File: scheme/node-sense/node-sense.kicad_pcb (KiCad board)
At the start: 2 copper layers, 33.5 x 33 mm, 20 parts, among them P1 Power, P10 CN, P11 CN, P12 CN, P13 CN, P2 CN, P3 CN, P4 CN, P6 CN, P8 CN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

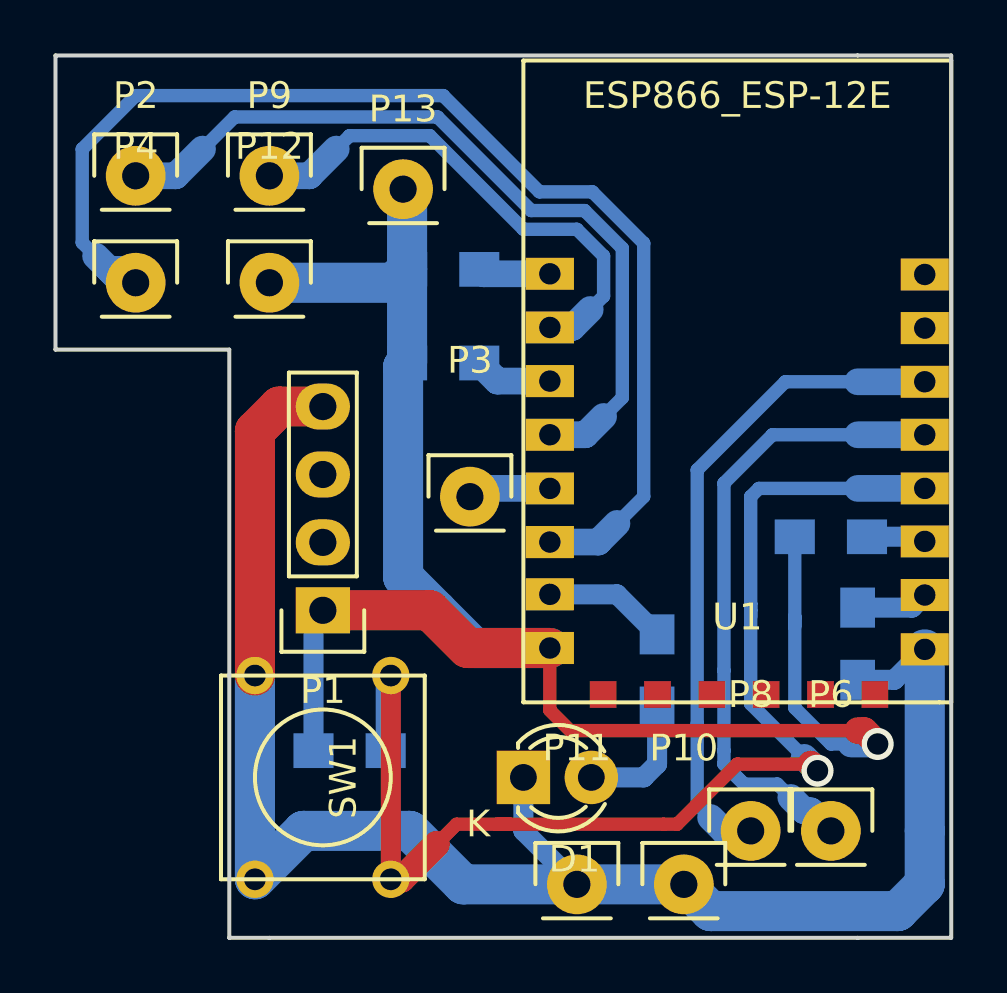
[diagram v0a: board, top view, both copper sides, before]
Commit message: node-sene: add more GND/Vcc pads, move tracks to front layer
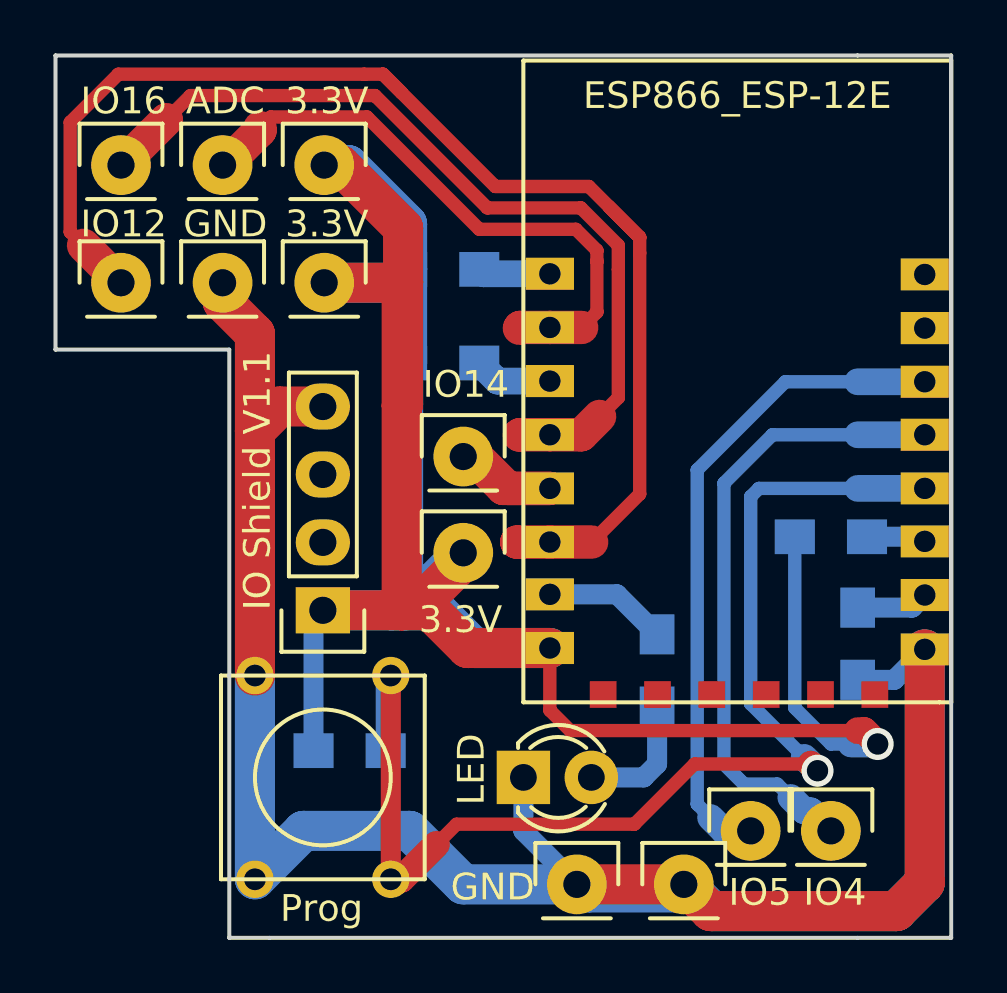
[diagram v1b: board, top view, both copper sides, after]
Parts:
- added P14: 3.3V, Pin_Headers:Pin_Header_Straight_1x01, F.Cu at (122.2, 81.6)
- added P15: GND, Pin_Headers:Pin_Header_Straight_1x01, F.Cu at (113.2, 71.5)
- P1: value Power -> (none)
- P10, P11: value CN -> GND
- P12, P13: value CN -> 3.3V
- P2: value CN -> IO16
- P3: value CN -> IO14
- P4: value CN -> IO12
- P6: value CN -> IO4
- P8: value CN -> IO5
- P9: value CN -> ADC
- moved P13 3.08 mm to (117.0, 67.1)
- moved P12 2.05 mm to (117.0, 71.5)
- moved P9 1.80 mm to (113.2, 67.1)
- moved P3 1.52 mm to (122.2, 78.0)
- moved P2 0.68 mm to (109.5, 67.1)
- moved P4 0.55 mm to (109.5, 71.5)
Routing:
- net /3.3Vcc: track 71.0 -> 104.8 mm
- net /GND: track 66.6 -> 95.4 mm
- net Net-(P3-Pad1): track 3.12 -> 7.17 mm
- net Net-(P9-Pad1): track 22.8 -> 24.3 mm
- net Net-(R4-Pad1): track 51.0 -> 50.0 mm
- net Net-(P2-Pad1): track 33.8 -> 32.9 mm
- net Net-(P4-Pad1): track 49.5 -> 48.9 mm
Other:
- board text added: "IO Shield V1.1"
